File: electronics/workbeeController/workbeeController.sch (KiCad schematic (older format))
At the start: 88 parts, among them J1 24V, J10 OUT C, J11 OUT D, J12 OUT E, J13 OUT F, J14 OUT G, J15 OUT H, J16 OUT I, J17 OUT J, J18 OUT K, J19 OUT L, J2 SR_OUT_EXT, J20 OUT M, J21 OUT N, J22 OUT O, J23 OUT P, J24 IN A, J25 IN B, J26 IN C, J27 IN D, J28 IN E, J29 IN F, J3 SR_IN_EXT, J30 IN G, J31 IN H, J32 ESTOP, J33 PROBE, J34 RS485, J35 24V, J36 5V, J37 3.3V, J38 GND, J4 PULSE, J5 GND, J6 3.3v, J7 GPIO, J8 OUT A, J9 OUT B, U1 74HC595, U10 PC817, U11 PC817, U12 PC817, U13 PC817, U14 PC817, U15 PC817, U16 PC817, U17 LevelShifterModule, U2 74HC595, U3 TTGO_TDisplay, U4 Buck, U5 74HC165, U6 SP485EN, U7 PC817, U8 PC817, U9 PC817

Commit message: PCB routed
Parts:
- removed JP1: Jumper_NC_Small, Jumper:SolderJumper-2_P1.3mm_Bridged_Pad1.0x1.5mm, symbol Device:Jumper_NC_Small
- added C6, C7: 0.1uF, Capacitor_THT:C_Disc_D5.0mm_W2.5mm_P2.50mm, symbol Device:C_Small
- added H5: MountingHole_Pad, MountingHole:MountingHole_4.3mm_M4_ISO7380_Pad, symbol Mechanical:MountingHole_Pad
- added J39: IN (INKL), Connector_PinSocket_2.54mm:PinSocket_1x04_P2.54mm_Vertical, symbol Connector:Conn_01x04_Female
- added J40: IN (MNOP), Connector_PinSocket_2.54mm:PinSocket_1x04_P2.54mm_Vertical, symbol Connector:Conn_01x04_Female
- added JP1: Omit Aux Shift Register (U18), Jumper:SolderJumper-2_P1.3mm_Open_TrianglePad1.0x1.5mm, symbol Device:Jumper_NO_Small
- added U18: 74HC165, Package_DIP:DIP-16_W7.62mm, symbol 74HC165:74HC165
- J10, J11, J12, J13, J14, J15, J16, J17, J18, J19, J20, J21, J22, J23, J8, J9: footprint Connector_PinHeader_2.54mm:PinHeader_1x02_P2.54mm_Vertical -> Connector_PinSocket_2.54mm:PinSocket_1x02_P2.54mm_Vertical; symbol Connector:Conn_01x02_Male -> Connector:Conn_01x02_Female
- J2, J3: symbol Connector:Conn_01x05_Female -> Connector:Conn_01x05_Male
- J24, J25, J26, J27, J28, J29, J30, J31, J32, J33: footprint Connector_PinHeader_2.54mm:PinHeader_1x02_P2.54mm_Vertical -> Connector_PinSocket_2.54mm:PinSocket_1x02_P2.54mm_Vertical
- J35, J36, J37, J38: footprint Connector_PinHeader_2.54mm:PinHeader_1x04_P2.54mm_Vertical -> Connector_PinSocket_2.54mm:PinSocket_1x04_P2.54mm_Vertical
- R34: value 220 -> 1k
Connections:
- net +3V3: now also J3.5 (Pin_5), R15.2, R20.2, C6.2, C7.1, U18.16 (VCC); no longer J3.1 (Pin_1)
- net GND: now also J3.1 (Pin_1), C6.1, C7.2, JP1.2, U18.15 (CLKIN), U18.8 (GND); no longer J3.5 (Pin_5)
- net SR_IN_CLOCK: now also U18.2 (CLK)
- net SR_IN_DATA2: now also U18.10 (SER); no longer U5.10 (SER)
- net SR_IN_LATCH: now also U18.1 (~LD)
- new net: JP1.1, U18.9 (QH), U5.10 (SER)
- new net IN_I: J39.1 (Pin_1), U18.11 (A)
- new net IN_J: J39.2 (Pin_2), U18.12 (B)
- new net IN_K: J39.3 (Pin_3), U18.13 (C)
- new net IN_L: J39.4 (Pin_4), U18.14 (D)
- new net IN_M: J40.1 (Pin_1), U18.3 (E)
- new net IN_N: J40.2 (Pin_2), U18.4 (F)
- new net IN_O: J40.3 (Pin_3), U18.5 (G)
- new net IN_P: J40.4 (Pin_4), U18.6 (H)
- no-connect marks 5 -> 7
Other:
- moved on the sheet: C1, C2, C3, C4, D3, D4, D5, J34, J35, J36, J37, J38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

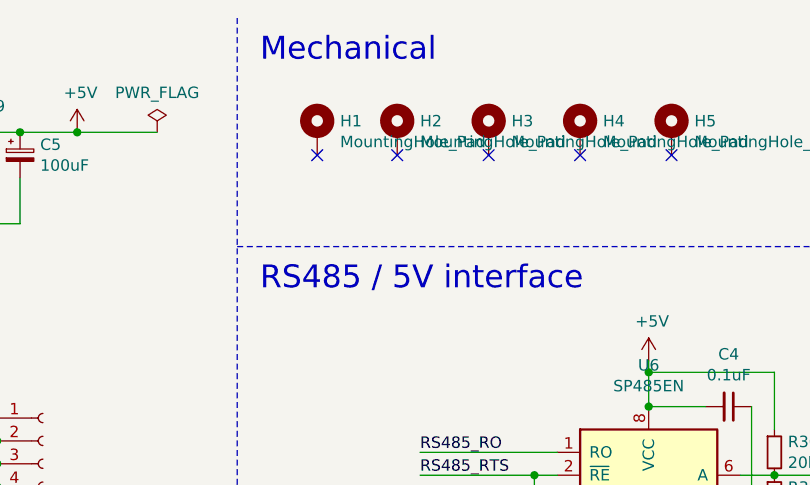
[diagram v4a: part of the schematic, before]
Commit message: Change resistor footprints, add ground/chassis jumper
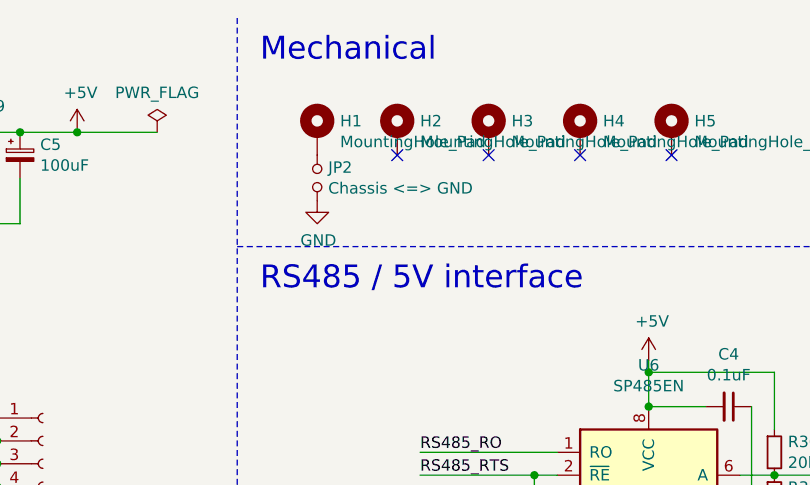
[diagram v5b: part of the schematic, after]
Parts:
- added JP2: Chassis <=> GND, Connector_PinHeader_2.54mm:PinHeader_1x02_P2.54mm_Vertical, symbol Device:Jumper_NO_Small
- R1, R10, R15, R20, R30, R31, R32, R33, R34, R35, R5: footprint Resistor_THT:R_Axial_DIN0207_L6.3mm_D2.5mm_P2.54mm_Vertical -> Resistor_THT:R_Axial_DIN0207_L6.3mm_D2.5mm_P7.62mm_Horizontal
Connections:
- net GND: now also JP2.1
- net at H1.1: now also JP2.2
- no-connect marks 7 -> 6
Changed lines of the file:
@@
 F 0 "R5" V 13704 6700 50  0000 C CNN
 F 1 "1k" V 13795 6700 50  0000 C CNN
-F 2 "Resistor_THT:R_Axial_DIN0207_L6.3mm_D2.5mm_P2.54mm_Vertical" H 13900 6700 50  0001 C CNN
+F 2 "Resistor_THT:R_Axial_DIN0207_L6.3mm_D2.5mm_P7.62mm_Horizontal" H 13900 6700 50  0001 C CNN
 F 3 "~" H 13900 6700 50  0001 C CNN
 	1    13900 6700
@@
 F 0 "R15" H 14941 6354 50  0000 R CNN
 F 1 "47k" H 14941 6445 50  0000 R CNN
-F 2 "Resistor_THT:R_Axial_DIN0207_L6.3mm_D2.5mm_P2.54mm_Vertical" H 15000 6400 50  0001 C CNN
+F 2 "Resistor_THT:R_Axial_DIN0207_L6.3mm_D2.5mm_P7.62mm_Horizontal" H 15000 6400 50  0001 C CNN
 F 3 "~" H 15000 6400 50  0001 C CNN
 	1    15000 6400
@@
 F 0 "R10" V 13704 7950 50  0000 C CNN
 F 1 "2.2k" V 13795 7950 50  0000 C CNN
-F 2 "Resistor_THT:R_Axial_DIN0207_L6.3mm_D2.5mm_P2.54mm_Vertical" H 13900 7950 50  0001 C CNN
+F 2 "Resistor_THT:R_Axial_DIN0207_L6.3mm_D2.5mm_P7.62mm_Horizontal" H 13900 7950 50  0001 C CNN
 F 3 "~" H 13900 7950 50  0001 C CNN
 	1    13900 7950
@@
 F 0 "R20" H 14941 7604 50  0000 R CNN
 F 1 "47k" H 14941 7695 50  0000 R CNN
-F 2 "Resistor_THT:R_Axial_DIN0207_L6.3mm_D2.5mm_P2.54mm_Vertical" H 15000 7650 50  0001 C CNN
+F 2 "Resistor_THT:R_Axial_DIN0207_L6.3mm_D2.5mm_P7.62mm_Horizontal" H 15000 7650 50  0001 C CNN
 F 3 "~" H 15000 7650 50  0001 C CNN
 	1    15000 7650
@@
 F 0 "R31" H 7609 2646 50  0000 L CNN
 F 1 "120" H 7609 2555 50  0000 L CNN
-F 2 "Resistor_THT:R_Axial_DIN0207_L6.3mm_D2.5mm_P2.54mm_Vertical" H 7550 2600 50  0001 C CNN
+F 2 "Resistor_THT:R_Axial_DIN0207_L6.3mm_D2.5mm_P7.62mm_Horizontal" H 7550 2600 50  0001 C CNN
 F 3 "~" H 7550 2600 50  0001 C CNN
 	1    7550 2600
@@
 F 0 "R30" H 7609 2446 50  0000 L CNN
 F 1 "20k" H 7609 2355 50  0000 L CNN
-F 2 "Resistor_THT:R_Axial_DIN0207_L6.3mm_D2.5mm_P2.54mm_Vertical" H 7550 2400 50  0001 C CNN
+F 2 "Resistor_THT:R_Axial_DIN0207_L6.3mm_D2.5mm_P7.62mm_Horizontal" H 7550 2400 50  0001 C CNN
 F 3 "~" H 7550 2400 50  0001 C CNN
 	1    7550 2400
@@
 F 0 "R32" H 7609 2846 50  0000 L CNN
 F 1 "20k" H 7609 2755 50  0000 L CNN
-F 2 "Resistor_THT:R_Axial_DIN0207_L6.3mm_D2.5mm_P2.54mm_Vertical" H 7550 2800 50  0001 C CNN
+F 2 "Resistor_THT:R_Axial_DIN0207_L6.3mm_D2.5mm_P7.62mm_Horizontal" H 7550 2800 50  0001 C CNN
 F 3 "~" H 7550 2800 50  0001 C CNN
 	1    7550 2800
@@
 F 0 "R33" H 909 2496 50  0000 L CNN
 F 1 "2.2k" H 909 2405 50  0000 L CNN
-F 2 "Resistor_THT:R_Axial_DIN0207_L6.3mm_D2.5mm_P2.54mm_Vertical" H 850 2450 50  0001 C CNN
+F 2 "Resistor_THT:R_Axial_DIN0207_L6.3mm_D2.5mm_P7.62mm_Horizontal" H 850 2450 50  0001 C CNN
 F 3 "~" H 850 2450 50  0001 C CNN
 	1    850  2450
@@
 F 0 "R34" H 1559 2496 50  0000 L CNN
 F 1 "1k" H 1559 2405 50  0000 L CNN
-F 2 "Resistor_THT:R_Axial_DIN0207_L6.3mm_D2.5mm_P2.54mm_Vertical" H 1500 2450 50  0001 C CNN
+F 2 "Resistor_THT:R_Axial_DIN0207_L6.3mm_D2.5mm_P7.62mm_Horizontal" H 1500 2450 50  0001 C CNN
 F 3 "~" H 1500 2450 50  0001 C CNN
 	1    1500 2450
@@
 F 0 "R35" H 2059 2496 50  0000 L CNN
 F 1 "220" H 2059 2405 50  0000 L CNN
-F 2 "Resistor_THT:R_Axial_DIN0207_L6.3mm_D2.5mm_P2.54mm_Vertical" H 2000 2450 50  0001 C CNN
+F 2 "Resistor_THT:R_Axial_DIN0207_L6.3mm_D2.5mm_P7.62mm_Horizontal" H 2000 2450 50  0001 C CNN
 F 3 "~" H 2000 2450 50  0001 C CNN
 	1    2000 2450
@@
 F 0 "R1" V 10604 3350 50  0000 C CNN
 F 1 "1k" V 10695 3350 50  0000 C CNN
-F 2 "Resistor_THT:R_Axial_DIN0207_L6.3mm_D2.5mm_P2.54mm_Vertical" H 10800 3350 50  0001 C CNN
+F 2 "Resistor_THT:R_Axial_DIN0207_L6.3mm_D2.5mm_P7.62mm_Horizontal" H 10800 3350 50  0001 C CNN
 F 3 "~" H 10800 3350 50  0001 C CNN
 	1    10800 3350
@@
 NoConn ~ 6300 1100
 NoConn ~ 5900 1100
-NoConn ~ 5550 1100
 $Comp
 L 74HC165:74HC165 U18
@@
 Wire Wire Line
 	7100 7600 7100 7700
+$Comp
+L Device:Jumper_NO_Small JP2
+U 1 1 600B1603
+P 5550 1200
+F 0 "JP2" V 5596 1152 50  0000 R CNN
+F 1 "Chassis <=> GND" V 5505 1152 50  0000 R CNN
+F 2 "Connector_PinHeader_2.54mm:PinHeader_1x02_P2.54mm_Vertical" H 5550 1200 50  0001 C CNN
+F 3 "~" H 5550 1200 50  0001 C CNN
+	1    5550 1200
+	0    -1   -1   0
+$EndComp
+$Comp
+L power:GND #PWR041
+U 1 1 600B2249
+P 5550 1300
+F 0 "#PWR041" H 5550 1050 50  0001 C CNN
+F 1 "GND" H 5555 1127 50  0000 C CNN
+F 2 "" H 5550 1300 50  0001 C CNN
+F 3 "" H 5550 1300 50  0001 C CNN
+	1    5550 1300
+	1    0    0    -1
+$EndComp
 $EndSCHEMATC
